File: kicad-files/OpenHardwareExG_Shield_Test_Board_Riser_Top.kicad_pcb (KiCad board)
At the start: 4 copper layers, 147.3 x 81.3 mm, 16 parts

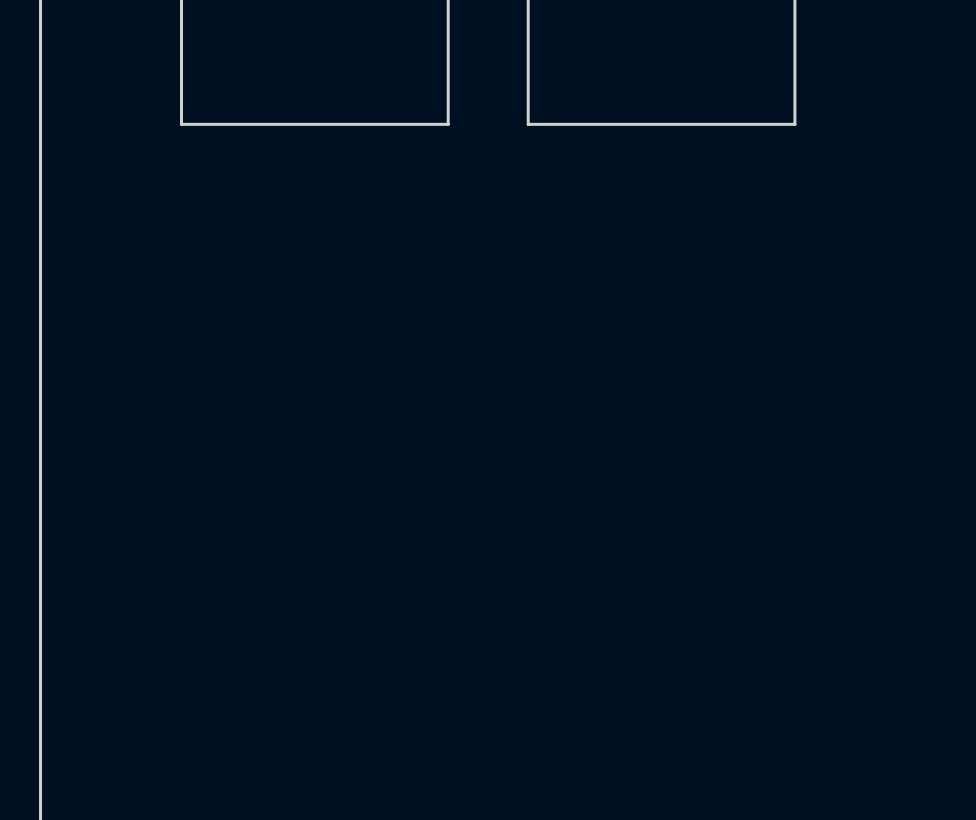
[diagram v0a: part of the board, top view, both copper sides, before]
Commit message: add extra set of tabs
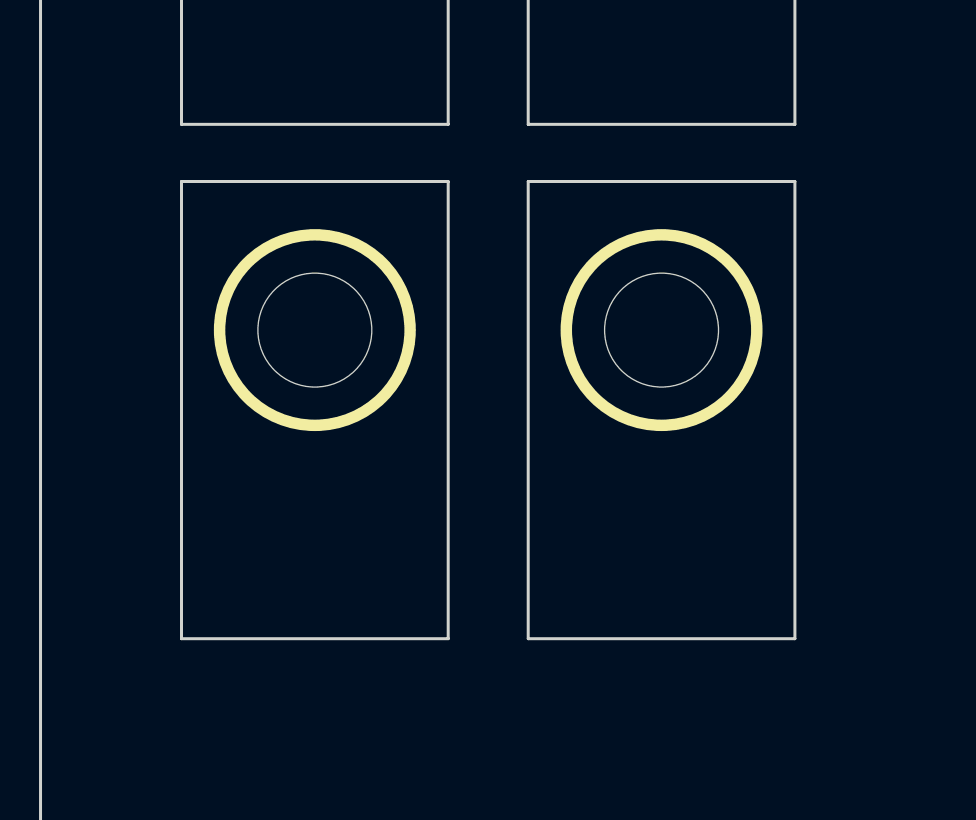
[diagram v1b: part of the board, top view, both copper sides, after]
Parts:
- added Hole_M3: VAL**, Hole_M3, F.Cu at (79.5, 71.1)
- added Hole_M3: VAL**, Hole_M3, F.Cu at (67.9, 71.1)
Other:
- outline, holes or cut-outs redrawn
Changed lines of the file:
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@@
     (area 48.209999 17.729999 195.630001 100.1776)
     (thickness 1.6)
-    (drawings 29)
+    (drawings 37)
     (tracks 0)
     (zones 0)
-    (modules 16)
+    (modules 18)
     (nets 1)
   )
@@
   )
   (module Hole_M3 (layer F.Cu)
+    (at 79.502 71.12)
+    (path Hole_M3)
+    (fp_text reference Hole_M3 (at 0 -4.445) (layer F.SilkS) hide
+      (effects (font (size 0.6 0.6) (thickness 0.127)))
+    )
+    (fp_text value VAL** (at 0 5.08) (layer F.SilkS) hide
+      (effects (font (size 1.524 1.524) (thickness 0.3048)))
+    )
+    (fp_circle (center 0 0) (end 0 3.175) (layer F.SilkS) (width 0.381))
+    (pad "" np_thru_hole circle (at 0 0) (size 3.7973 3.7973) (drill 3.7973)
+      (layers *.Cu *.Mask F.SilkS)
+    )
+  )
+  (module Hole_M3 (layer F.Cu)
+    (at 67.945 71.12)
+    (path Hole_M3)
+    (fp_text reference Hole_M3 (at 0 -4.445) (layer F.SilkS) hide
+      (effects (font (size 0.6 0.6) (thickness 0.127)))
+    )
+    (fp_text value VAL** (at 0 5.08) (layer F.SilkS) hide
+      (effects (font (size 1.524 1.524) (thickness 0.3048)))
+    )
+    (fp_circle (center 0 0) (end 0 3.175) (layer F.SilkS) (width 0.381))
+    (pad "" np_thru_hole circle (at 0 0) (size 3.7973 3.7973) (drill 3.7973)
+      (layers *.Cu *.Mask F.SilkS)
+    )
+  )
+  (module Hole_M3 (layer F.Cu)
     (at 67.945 53.975)
     (path Hole_M3)
@@
     )
   )
+  (gr_line (start 75.057 66.167) (end 83.947 66.167) (angle 90) (layer Edge.Cuts) (width 0.1))
+  (gr_line (start 83.947 66.167) (end 83.947 81.407) (angle 90) (layer Edge.Cuts) (width 0.1))
+  (gr_line (start 83.947 81.407) (end 75.057 81.407) (angle 90) (layer Edge.Cuts) (width 0.1))
+  (gr_line (start 75.057 81.407) (end 75.057 66.167) (angle 90) (layer Edge.Cuts) (width 0.1))
+  (gr_line (start 63.5 81.407) (end 63.5 66.167) (angle 90) (layer Edge.Cuts) (width 0.1))
+  (gr_line (start 72.39 81.407) (end 63.5 81.407) (angle 90) (layer Edge.Cuts) (width 0.1))
+  (gr_line (start 72.39 66.167) (end 72.39 81.407) (angle 90) (layer Edge.Cuts) (width 0.1))
+  (gr_line (start 63.5 66.167) (end 72.39 66.167) (angle 90) (layer Edge.Cuts) (width 0.1))
   (gr_line (start 63.5 49.022) (end 72.39 49.022) (angle 90) (layer Edge.Cuts) (width 0.1))
   (gr_line (start 72.39 49.022) (end 72.39 64.262) (angle 90) (layer Edge.Cuts) (width 0.1))
